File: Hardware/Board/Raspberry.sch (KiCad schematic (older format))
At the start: 1 part

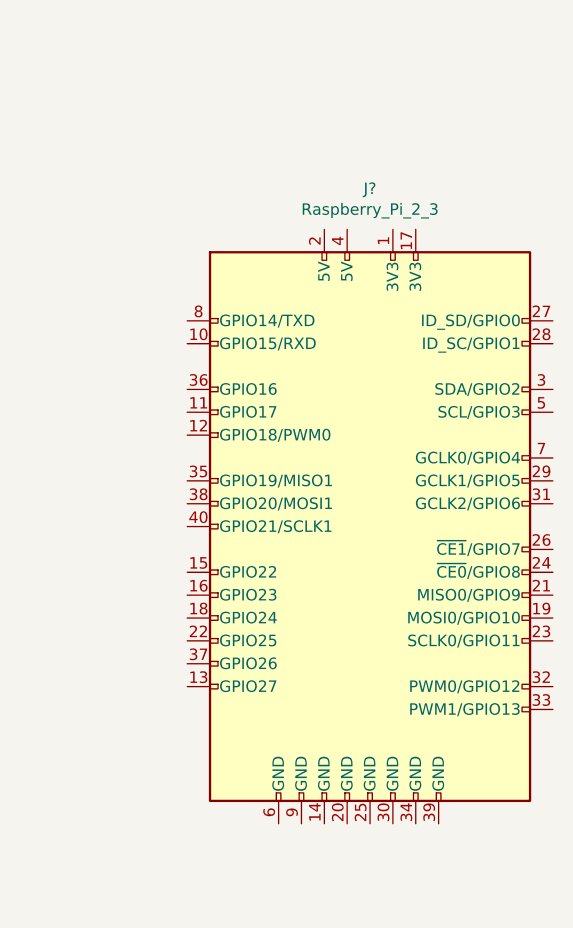
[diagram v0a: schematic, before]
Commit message: Schaltregler Design fertig gestellt, Datenblätter hinzu gefügt.
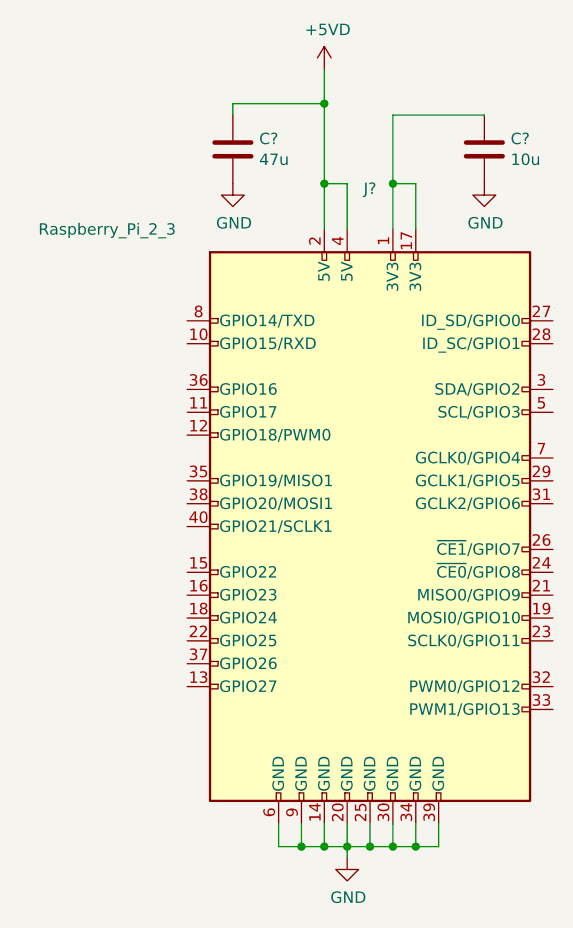
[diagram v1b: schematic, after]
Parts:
- added C?: 47u, symbol Device:C
- added C?: 10u, symbol Device:C
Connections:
- net at J?.1 (3V3): now also J?.17 (3V3), C?.1
- net GND: now reaches J?.14 (GND)
- net GND: now also J?.20 (GND), J?.25 (GND), J?.30 (GND), J?.34 (GND), J?.39 (GND), J?.6 (GND), J?.9 (GND), C?.2, C?.2
- net +5VD: now reaches J?.2 (5V)
- net +5VD: now also J?.4 (5V), C?.1
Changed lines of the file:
@@
 P 4400 3300
 F 0 "J?" H 4400 4778 50  0000 C CNN
-F 1 "Raspberry_Pi_2_3" H 4400 4687 50  0000 C CNN
+F 1 "Raspberry_Pi_2_3" H 3250 4600 50  0000 C CNN
 F 2 "" H 4400 3300 50  0001 C CNN
 F 3 "https://www.raspberrypi.org/documentation/hardware/raspberrypi/schematics/rpi_SCH_3bplus_1p0_reduced.pdf" H 4400 3300 50  0001 C CNN
@@
 	1    0    0    -1
 $EndComp
+$Comp
+L power:GND #PWR?
+U 1 1 5CC01696
+P 4300 4750
+F 0 "#PWR?" H 4300 4500 50  0001 C CNN
+F 1 "GND" H 4305 4577 50  0000 C CNN
+F 2 "" H 4300 4750 50  0001 C CNN
+F 3 "" H 4300 4750 50  0001 C CNN
+	1    4300 4750
+	1    0    0    -1
+$EndComp
+Wire Wire Line
+	4300 4600 4300 4700
+Wire Wire Line
+	4700 4600 4700 4700
+Wire Wire Line
+	4700 4700 4600 4700
+Connection ~ 4300 4700
+Wire Wire Line
+	4300 4700 4300 4750
+Wire Wire Line
+	4000 4600 4000 4700
+Wire Wire Line
+	4000 4700 4100 4700
+Wire Wire Line
+	4100 4600 4100 4700
+Connection ~ 4100 4700
+Wire Wire Line
+	4100 4700 4200 4700
+Wire Wire Line
+	4200 4600 4200 4700
+Connection ~ 4200 4700
+Wire Wire Line
+	4200 4700 4300 4700
+Wire Wire Line
+	4400 4600 4400 4700
+Connection ~ 4400 4700
+Wire Wire Line
+	4400 4700 4300 4700
+Wire Wire Line
+	4500 4600 4500 4700
+Connection ~ 4500 4700
+Wire Wire Line
+	4500 4700 4400 4700
+Wire Wire Line
+	4600 4600 4600 4700
+Connection ~ 4600 4700
+Wire Wire Line
+	4600 4700 4500 4700
+$Comp
+L power:+5VD #PWR?
+U 1 1 5CC0193E
+P 4200 1300
+F 0 "#PWR?" H 4200 1150 50  0001 C CNN
+F 1 "+5VD" H 4215 1473 50  0000 C CNN
+F 2 "" H 4200 1300 50  0001 C CNN
+F 3 "" H 4200 1300 50  0001 C CNN
+	1    4200 1300
+	1    0    0    -1
+$EndComp
+$Comp
+L Device:C C?
+U 1 1 5CC01965
+P 3800 1650
+F 0 "C?" H 3915 1696 50  0000 L CNN
+F 1 "47u" H 3915 1605 50  0000 L CNN
+F 2 "" H 3838 1500 50  0001 C CNN
+F 3 "~" H 3800 1650 50  0001 C CNN
+	1    3800 1650
+	1    0    0    -1
+$EndComp
+$Comp
+L Device:C C?
+U 1 1 5CC019EB
+P 4900 1650
+F 0 "C?" H 5015 1696 50  0000 L CNN
+F 1 "10u" H 5015 1605 50  0000 L CNN
+F 2 "" H 4938 1500 50  0001 C CNN
+F 3 "~" H 4900 1650 50  0001 C CNN
+	1    4900 1650
+	1    0    0    -1
+$EndComp
+$Comp
+L power:GND #PWR?
+U 1 1 5CC01A3B
+P 3800 1800
+F 0 "#PWR?" H 3800 1550 50  0001 C CNN
+F 1 "GND" H 3805 1627 50  0000 C CNN
+F 2 "" H 3800 1800 50  0001 C CNN
+F 3 "" H 3800 1800 50  0001 C CNN
+	1    3800 1800
+	1    0    0    -1
+$EndComp
+$Comp
+L power:GND #PWR?
+U 1 1 5CC01B10
+P 4900 1800
+F 0 "#PWR?" H 4900 1550 50  0001 C CNN
+F 1 "GND" H 4905 1627 50  0000 C CNN
+F 2 "" H 4900 1800 50  0001 C CNN
+F 3 "" H 4900 1800 50  0001 C CNN
+	1    4900 1800
+	1    0    0    -1
+$EndComp
+Wire Wire Line
+	4900 1500 4500 1500
+Wire Wire Line
+	4500 1500 4500 1800
+Wire Wire Line
+	4600 2000 4600 1800
+Wire Wire Line
+	4600 1800 4500 1800
+Connection ~ 4500 1800
+Wire Wire Line
+	4500 1800 4500 2000
+Wire Wire Line
+	4200 2000 4200 1800
+Wire Wire Line
+	4300 2000 4300 1800
+Wire Wire Line
+	4300 1800 4200 1800
+Connection ~ 4200 1800
+Wire Wire Line
+	4200 1800 4200 1450
+Wire Wire Line
+	3800 1500 3800 1450
+Wire Wire Line
+	3800 1450 4200 1450
+Connection ~ 4200 1450
+Wire Wire Line
+	4200 1450 4200 1300
 $EndSCHEMATC

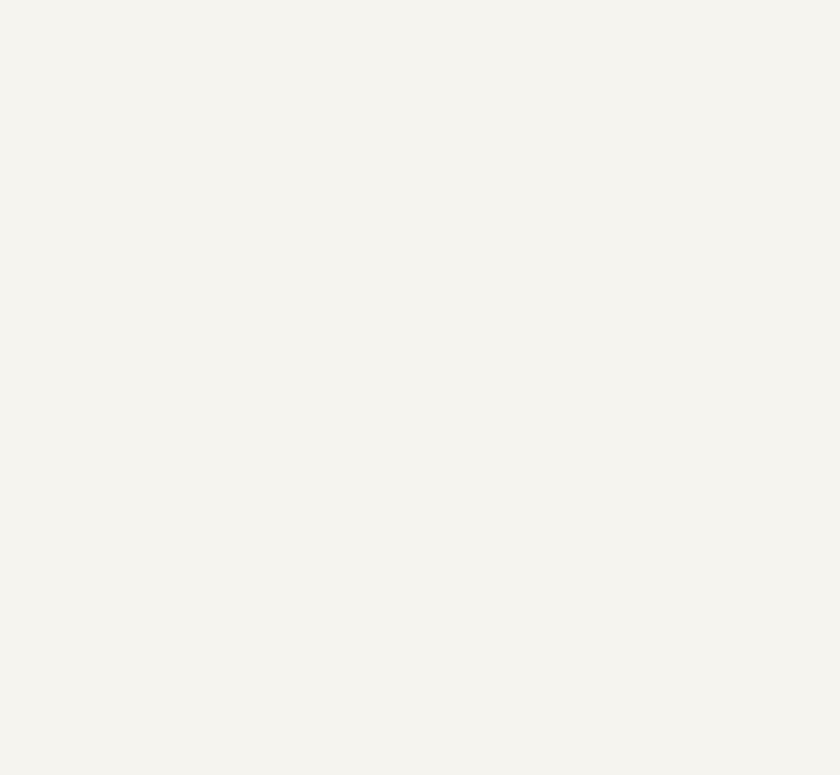
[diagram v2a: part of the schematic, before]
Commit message: 1Wire Power Pull Up. ESP Modul added
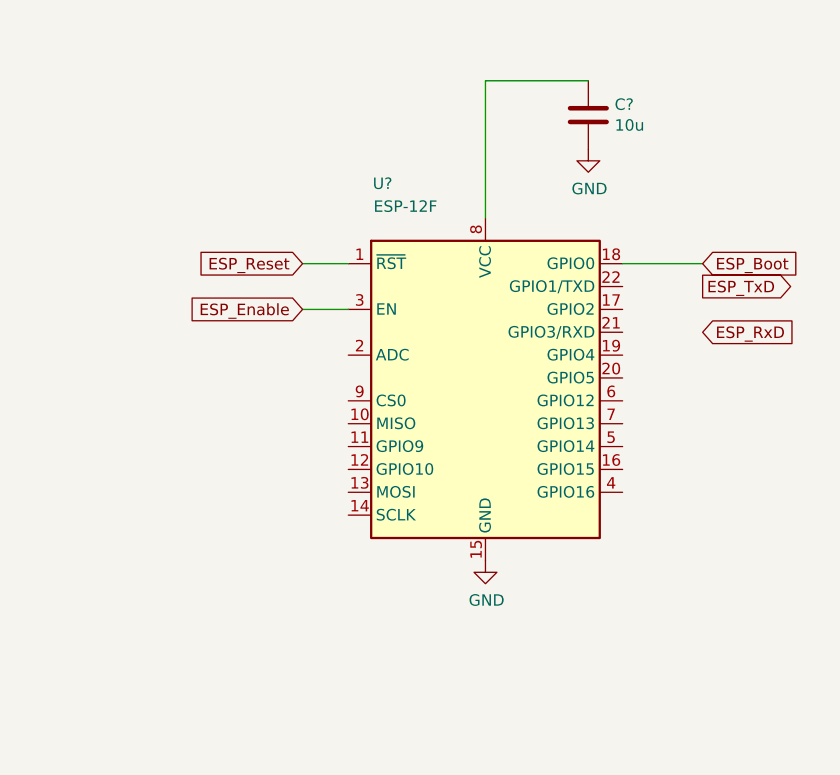
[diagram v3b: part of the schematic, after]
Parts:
- added C?: 10u, symbol Device:C
- added U?: ESP-12F, RF_Module:ESP-12E, symbol RF_Module:ESP-12F
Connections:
- net GND: now also C?.2, U?.15 (GND)
- new net: C?.1, U?.8 (VCC)
- new net ESP_Boot: U?.18 (GPIO0)
- new net ESP_Enable: U?.3 (EN)
- new net ESP_Reset: U?.1 (~RST)
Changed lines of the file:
@@
 Wire Wire Line
 	4200 1450 4200 1300
+$Comp
+L RF_Module:ESP-12F U?
+U 1 1 5CAB8BB3
+P 7950 2750
+F 0 "U?" H 7500 3700 50  0000 C CNN
+F 1 "ESP-12F" H 7600 3600 50  0000 C CNN
+F 2 "RF_Module:ESP-12E" H 7950 2750 50  0001 C CNN
+F 3 "http://wiki.ai-thinker.com/_media/esp8266/esp8266_series_modules_user_manual_v1.1.pdf" H 7600 2850 50  0001 C CNN
+	1    7950 2750
+	1    0    0    -1
+$EndComp
+Text GLabel 8900 2150 2    50   Input ~ 0
+ESP_Boot
+Text GLabel 8900 2250 2    50   Output ~ 0
+ESP_TxD
+Text GLabel 8900 2450 2    50   Input ~ 0
+ESP_RxD
+Text GLabel 7150 2150 0    50   Input ~ 0
+ESP_Reset
+Text GLabel 7150 2350 0    50   Input ~ 0
+ESP_Enable
+$Comp
+L Device:C C?
+U 1 1 5CB2F4A7
+P 8400 1500
+F 0 "C?" H 8515 1546 50  0000 L CNN
+F 1 "10u" H 8515 1455 50  0000 L CNN
+F 2 "" H 8438 1350 50  0001 C CNN
+F 3 "~" H 8400 1500 50  0001 C CNN
+	1    8400 1500
+	1    0    0    -1
+$EndComp
+$Comp
+L power:GND #PWR?
+U 1 1 5CB2F4AE
+P 8400 1650
+F 0 "#PWR?" H 8400 1400 50  0001 C CNN
+F 1 "GND" H 8405 1477 50  0000 C CNN
+F 2 "" H 8400 1650 50  0001 C CNN
+F 3 "" H 8400 1650 50  0001 C CNN
+	1    8400 1650
+	1    0    0    -1
+$EndComp
+$Comp
+L power:GND #PWR?
+U 1 1 5CB2F86B
+P 7950 3450
+F 0 "#PWR?" H 7950 3200 50  0001 C CNN
+F 1 "GND" H 7955 3277 50  0000 C CNN
+F 2 "" H 7950 3450 50  0001 C CNN
+F 3 "" H 7950 3450 50  0001 C CNN
+	1    7950 3450
+	1    0    0    -1
+$EndComp
+Wire Wire Line
+	7150 2150 7350 2150
+Wire Wire Line
+	7150 2350 7350 2350
+Wire Wire Line
+	8550 2150 8900 2150
+Wire Wire Line
+	7950 1950 7950 1350
+Wire Wire Line
+	7950 1350 8400 1350
 $EndSCHEMATC
